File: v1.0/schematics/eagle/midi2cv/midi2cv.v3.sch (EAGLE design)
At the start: 45 parts, among them IC1 PIC18F2431DIP, IC2 TL084P, IC3 TL084P, IC4 TL082P, J1 VEL3 OUT, J10 GATE4 OUT, J2 MOD1 OUT, J3 VEL1 OUT, J4 GATE5 OUT, J7 GATE1 OUT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

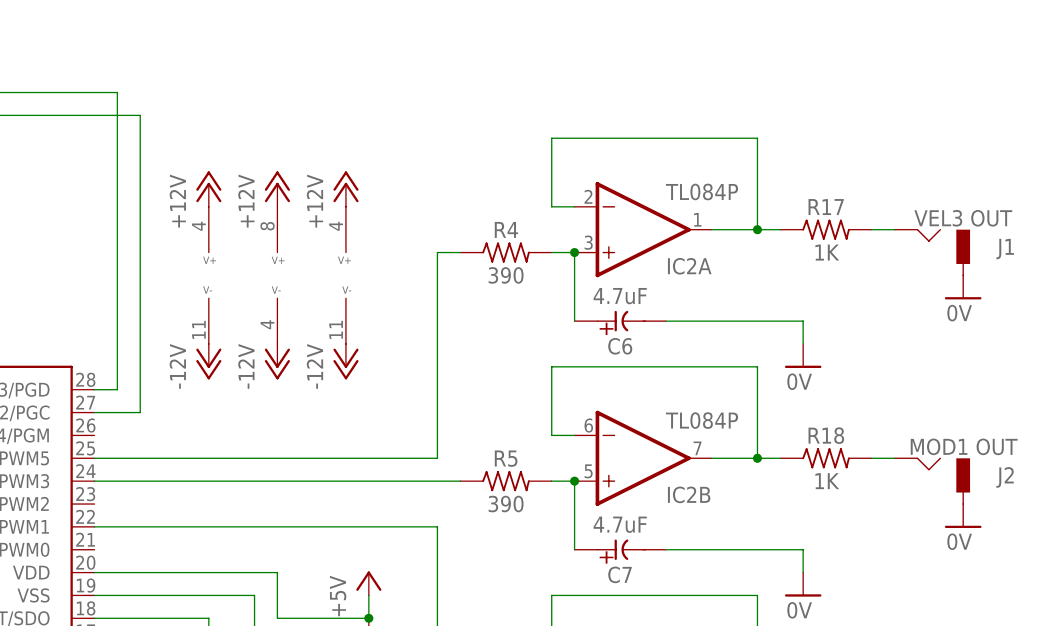
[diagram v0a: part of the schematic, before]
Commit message: Updated label on VEL2
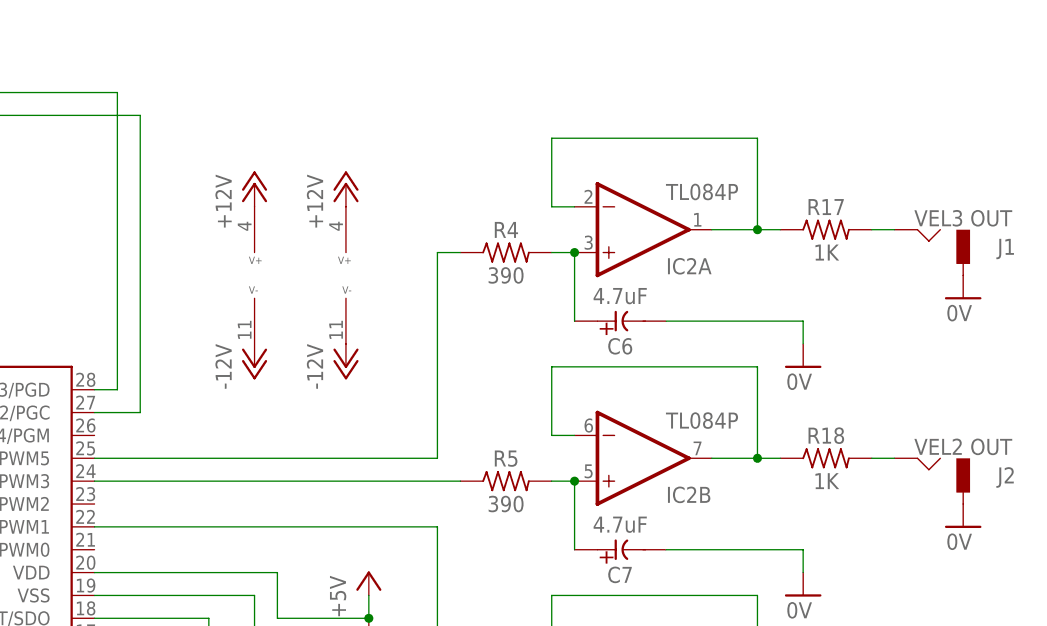
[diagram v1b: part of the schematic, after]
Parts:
- removed IC4: TL082P, _common:TL082P
- J2: value MOD1 OUT -> VEL2 OUT
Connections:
- net +12V: no longer IC4P.V+
- net -12V: no longer IC4P.V-
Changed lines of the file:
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@@
 <part name="P-1" library="supply1" deviceset="-12V" device=""/>
 <part name="J1" library="_common" deviceset="JACK-M" device="" value="VEL3 OUT"/>
-<part name="J2" library="_common" deviceset="JACK-M" device="" value="MOD1 OUT"/>
+<part name="J2" library="_common" deviceset="JACK-M" device="" value="VEL2 OUT"/>
 <part name="J3" library="_common" deviceset="JACK-M" device="" value="VEL1 OUT"/>
 <part name="J4" library="_common" deviceset="JACK-M" device="" value="GATE5 OUT"/>
@@
 <part name="C8" library="_common" deviceset="CE-US" device="E2-5" value="4.7uF"/>
 <part name="IC3" library="_common" deviceset="TL084" device="P"/>
-<part name="IC4" library="_common" deviceset="TL082" device="P"/>
-<part name="P+6" library="supply1" deviceset="+12V" device=""/>
 <part name="P+7" library="supply1" deviceset="+12V" device=""/>
-<part name="P-2" library="supply1" deviceset="-12V" device=""/>
 <part name="P-3" library="supply1" deviceset="-12V" device=""/>
 <part name="R10" library="_common" deviceset="R" device="0309/10" value="390"/>
@@
 <instance part="IC3" gate="C" x="-17.78" y="99.06" rot="R180"/>
 <instance part="IC3" gate="D" x="-17.78" y="81.28" rot="R180"/>
-<instance part="IC4" gate="P" x="114.3" y="86.36"/>
-<instance part="IC3" gate="P" x="106.68" y="86.36"/>
-<instance part="P+6" gate="1" x="114.3" y="96.52"/>
-<instance part="P+7" gate="1" x="106.68" y="96.52"/>
-<instance part="P-2" gate="1" x="114.3" y="76.2"/>
-<instance part="P-3" gate="1" x="106.68" y="76.2"/>
+<instance part="IC3" gate="P" x="111.76" y="86.36"/>
+<instance part="P+7" gate="1" x="111.76" y="96.52"/>
+<instance part="P-3" gate="1" x="111.76" y="76.2"/>
 <instance part="R10" gate="G$1" x="-2.54" y="132.08"/>
 <instance part="R11" gate="G$1" x="-2.54" y="114.3"/>
@@
 </segment>
 <segment>
-<pinref part="IC4" gate="P" pin="V+"/>
-<pinref part="P+6" gate="1" pin="+12V"/>
-</segment>
-<segment>
 <pinref part="IC3" gate="P" pin="V+"/>
 <pinref part="P+7" gate="1" pin="+12V"/>
@@
 </segment>
 <segment>
-<pinref part="IC4" gate="P" pin="V-"/>
-<pinref part="P-2" gate="1" pin="-12V"/>
-</segment>
-<segment>

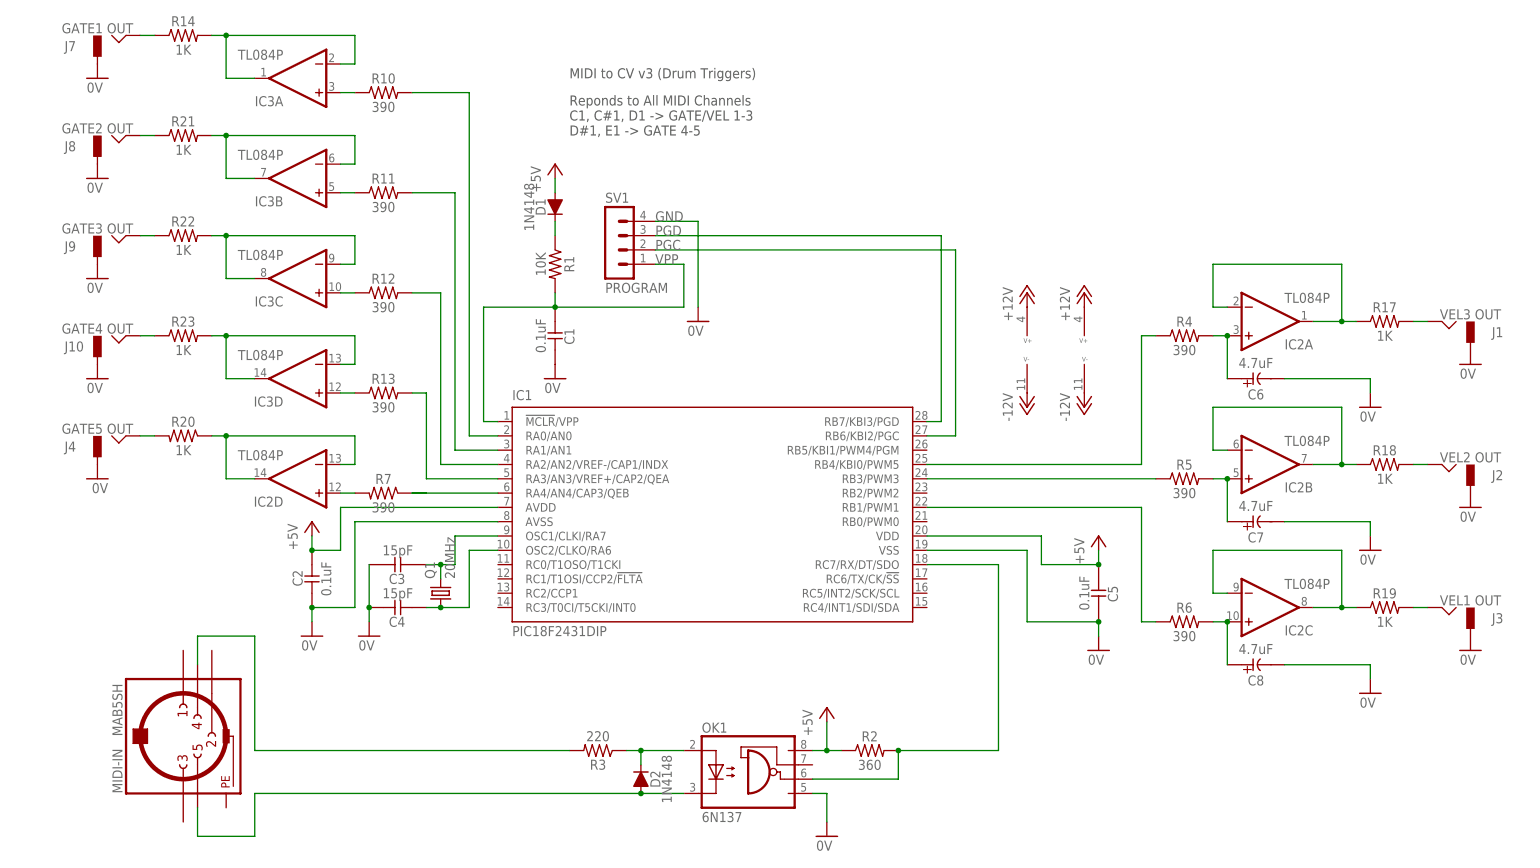
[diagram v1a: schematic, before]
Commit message: Update v3 with new multi-mode def's Implemented MODE0 (MODE1 still to come)
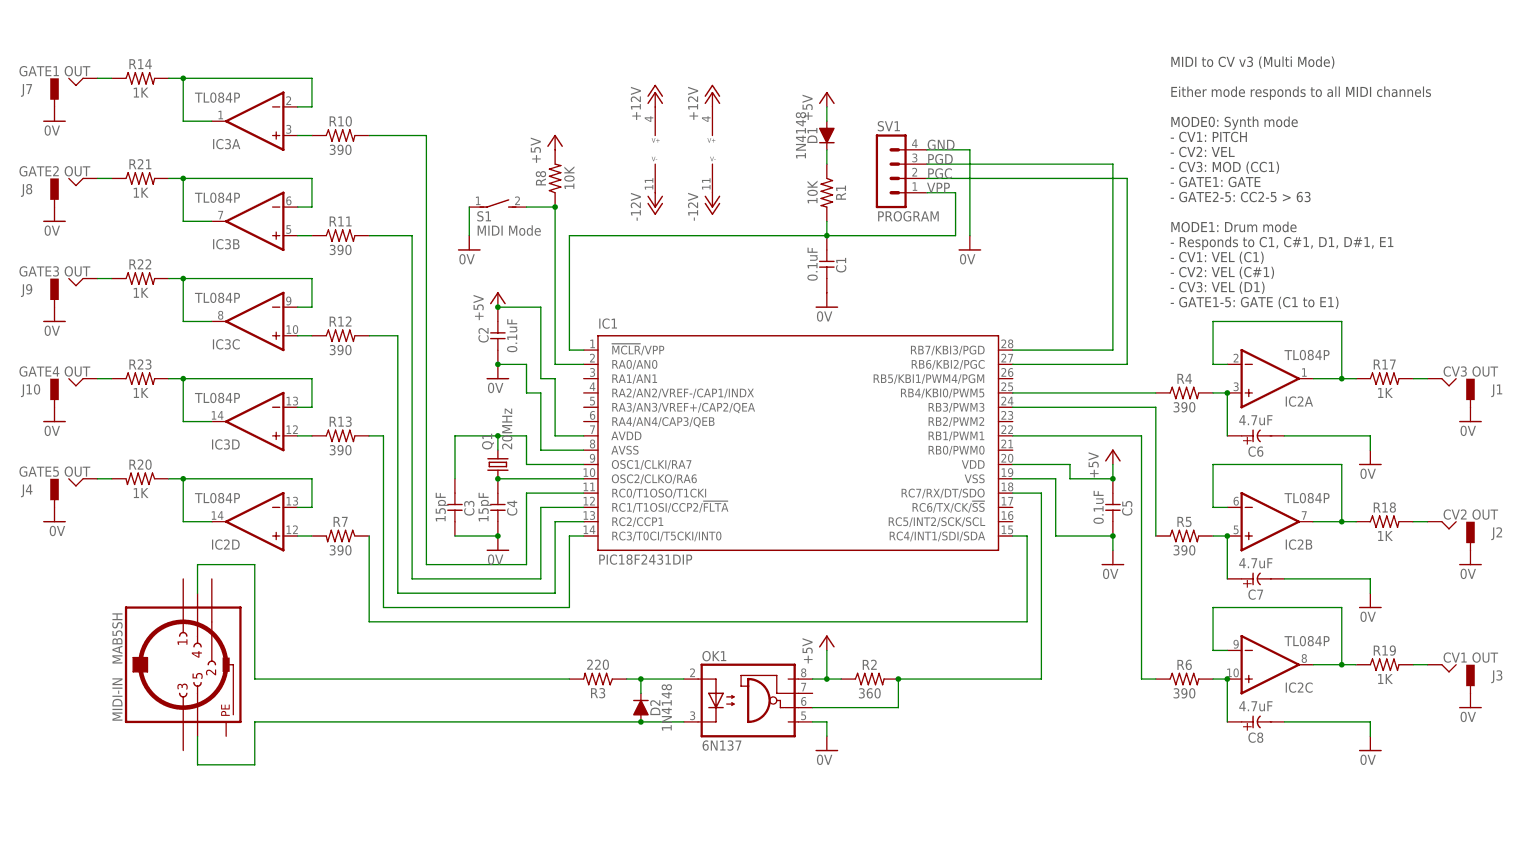
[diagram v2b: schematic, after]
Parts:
- added R8: 10K, _common:R0309/10
- added S1: MIDI Mode, switch-dil:DS01E
- J1: value VEL3 OUT -> CV3 OUT
- J2: value VEL2 OUT -> CV2 OUT
- J3: value VEL1 OUT -> CV1 OUT
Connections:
- new net N$20: IC1.RA0/AN0, R8.1, S1.2
- net +5V: now also R8.2
- net 0V: now also S1.1
- net N$13: now also IC1.RC7/RX/DT/SDO
- net N$19: now also IC1.RC4/INT1/SDI/SDA; no longer IC1.RA4/AN4/CAP3/QEB
- net N$26: now also IC1.RC0/T1OSO/T1CKI; no longer IC1.RA0/AN0
- net N$28: now also IC1.RC1/T1OSI/CCP2/!FLTA; no longer IC1.RA1/AN1
- net N$29: now also IC1.RC2/CCP1; no longer IC1.RA2/AN2/VREF-/CAP1/INDX
- net N$30: now also IC1.RC3/T0CI/T5CKI/INT0; no longer IC1.RA3/AN3/VREF+/CAP2/QEA
- net N$6: now also IC1.OSC2/CLKO/RA6
- net PGC: now also IC1.RB6/KBI2/PGC
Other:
- note added: "MIDI to CV v3 (Multi Mode) Either mode responds to all MIDI channels MODE0: Synth mode - CV1: PITCH - CV2: VEL - CV3: MOD (CC1) - GATE1: GATE - GATE2-5: CC2-5 > 63 MODE1: Drum mode - Responds to C1, C#1, D1, D#1, E1 - CV1: VEL (C1) - CV2: VEL (C#1) - CV3: VEL (D1) - GATE1-5: GATE (C1 to E1)"
- note removed: "MIDI to CV v3 (Drum Triggers)"
- note removed: "Reponds to All MIDI Channels C1, C#1, D1 -> GATE/VEL 1-3 D#1, E1 -> GATE 4-5"
- moved on the sheet: C1, C2, C3, C4, C5, C6, C7, C8, D1, D2, IC1, IC2A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
